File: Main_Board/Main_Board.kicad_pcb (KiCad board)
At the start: 4 copper layers, 66 parts, among them IC1 AZ1085CD-3.3TRG1, J1 PJ-037A, U1 STM32L152ZCTx, U2 LM386, Y1 ABM10W-16.0000MHZ-4-B1U-T3

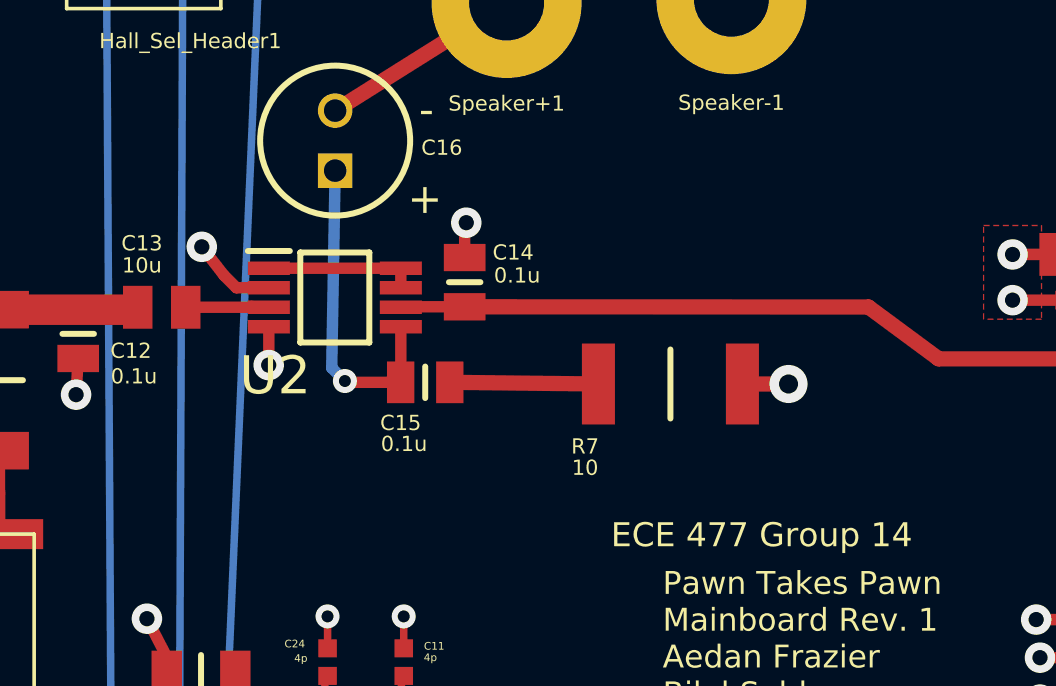
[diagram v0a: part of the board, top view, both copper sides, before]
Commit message: changed LM386 package to match what I bought
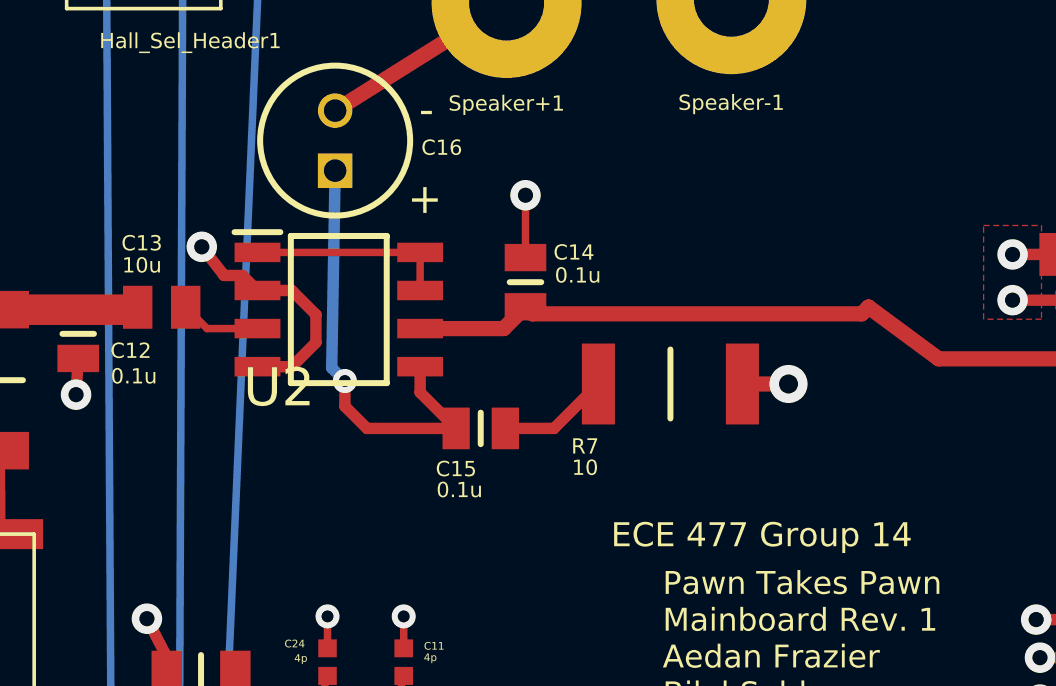
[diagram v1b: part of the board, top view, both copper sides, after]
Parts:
- U2: footprint SamacSys_Parts:SOP65P490X110-8N -> SamacSys_Parts:SOIC127P600X175-8N
- moved C15 2.41 mm to (120.4, 42.1)
- moved C14 2.03 mm to (121.9, 37.2)
- moved U2 0.42 mm to (115.7, 38.1)
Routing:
- net GND: track 154.7 -> 159.4 mm, vias 44 -> 43
- net Net-(C15-Pad1): track 10.9 -> 14.7 mm
- net NC: track 5.05 -> 6.69 mm
- net Net-(C15-Pad2): track 5.08 -> 3.84 mm

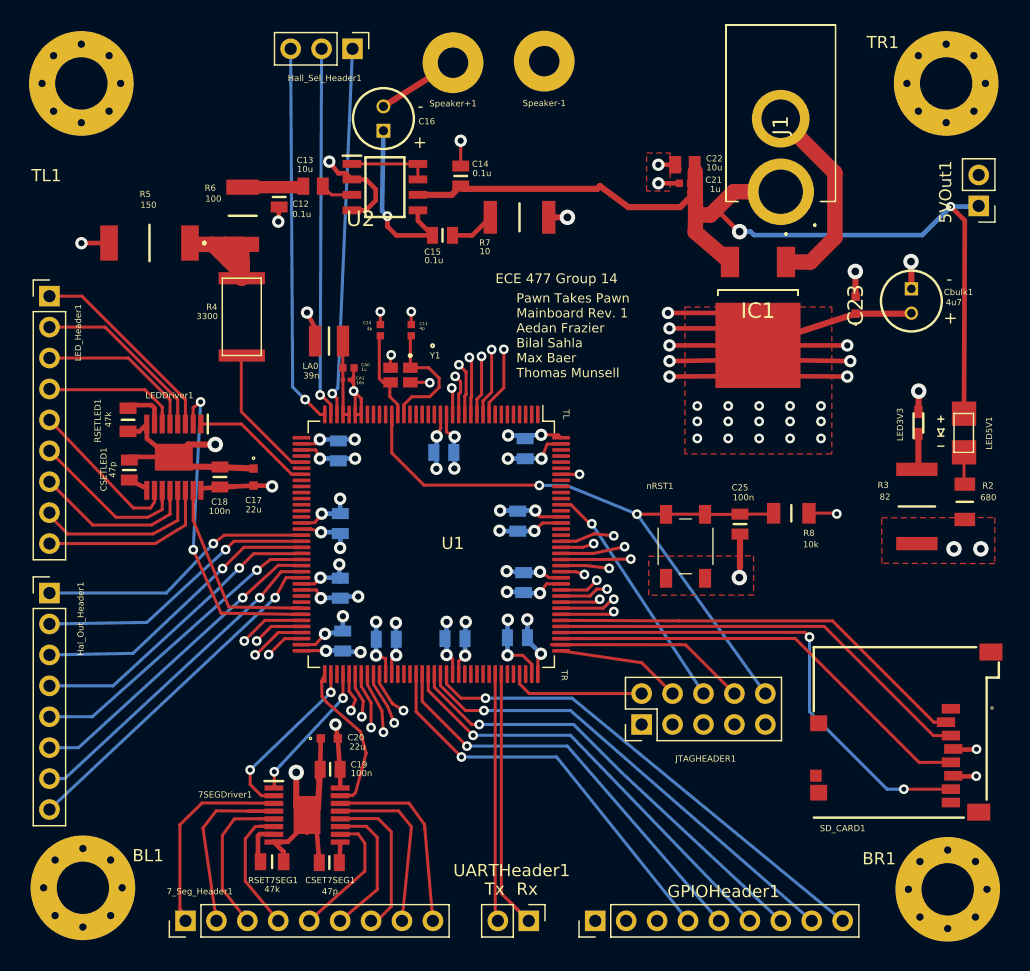
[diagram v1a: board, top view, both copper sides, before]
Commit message: changed board outline
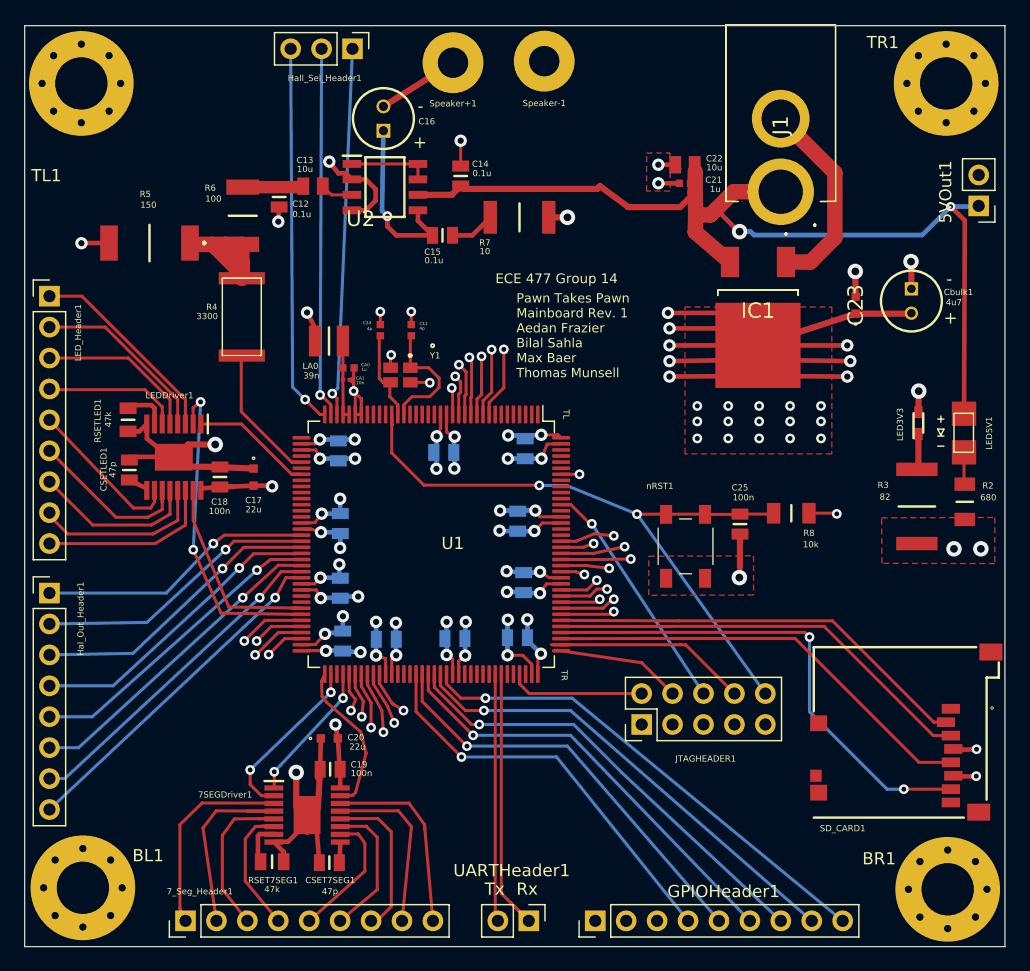
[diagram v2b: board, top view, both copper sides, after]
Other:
- board outline added: 80.5 x 75.6 mm
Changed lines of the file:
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@@
   (general
     (thickness 1.6)
-    (drawings 15)
+    (drawings 19)
     (tracks 847)
     (zones 0)
@@
     (38 B.Mask user)
     (39 F.Mask user)
-    (40 Dwgs.User user)
+    (40 Dwgs.User user hide)
     (41 Cmts.User user)
     (42 Eco1.User user hide)
@@
     )
   )
+  (gr_line (start 86.106 100.4824) (end 86.106 24.8412) (layer Edge.Cuts) (width 0.05))
+  (gr_line (start 166.624 100.4824) (end 86.106 100.4824) (layer Edge.Cuts) (width 0.05))
+  (gr_line (start 166.624 24.8412) (end 166.624 100.4824) (layer Edge.Cuts) (width 0.05))
+  (gr_line (start 86.106 24.8412) (end 166.624 24.8412) (layer Edge.Cuts) (width 0.05))
   (gr_text "ECE 477 Group 14" (at 129.794 45.6184) (layer F.SilkS)
     (effects (font (size 0.8 0.8) (thickness 0.15)))

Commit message: Schem Pictures
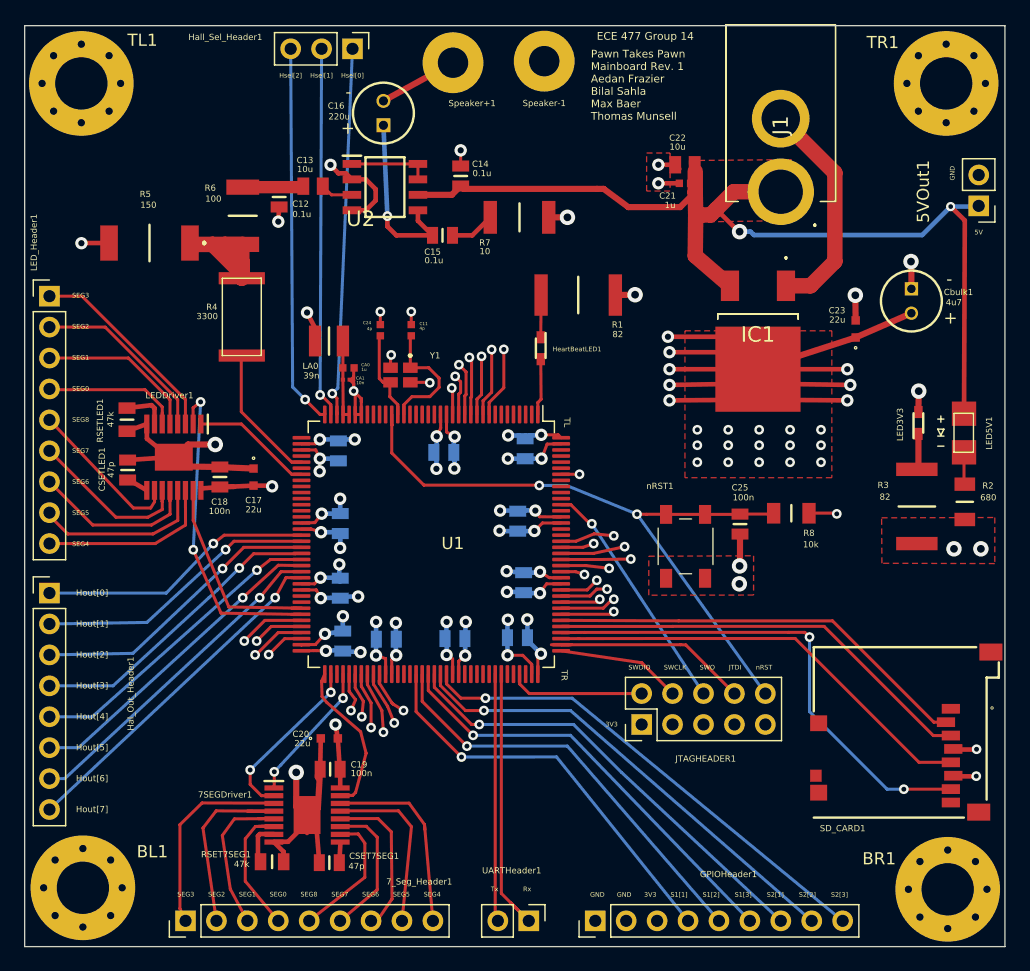
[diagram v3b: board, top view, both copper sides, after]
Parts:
- added HeartBeatLED1: HeartBeatLED, LEDM168X65N, F.Cu at (128.5, 51.3)
- added R1: 82, RESC6432X65N, F.Cu at (131.6, 47.0)
- nRST1: value PTS647SM50SMTR2LFS -> A
- moved C23 1.96 mm to (154.4, 49.8)
- moved IC1 1.96 mm to (146.3, 51.6)
- moved C16 0.45 mm to (115.6, 33.0)
- moved CSETLED1 0.14 mm to (94.6, 61.3)
- moved RSETLED1 0.09 mm to (94.5, 57.2)
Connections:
- U1 pad 1: Net-(U1-Pad1) -> HeartbeatLED
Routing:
- net HeartbeatLED: track 0.00 -> 4.65 mm
- net Net-(HeartBeatLED1-Pad1): track 0.00 -> 3.47 mm
- net GND: track 159.4 -> 162.0 mm, vias 43 -> 45
- net +5V: track 81.8 -> 83.6 mm
- net Net-(C16-Pad2): track 7.05 -> 6.52 mm
- added copper zone on F.Cu, net +5V
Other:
- board text added: "3V3"
- board text added: "5V"
- board text added: "GND"
- board text added: "Hout[0]"
- board text added: "Hout[1]"
- board text added: "Hout[2]"
- board text added: "Hout[3]"
- board text added: "Hout[4]"
- board text added: "Hout[5]"
- board text added: "Hout[6]"
- board text added: "Hout[7]"
- board text added: "Hsel[0]"
- board text added: "Hsel[1]"
- board text added: "Hsel[2]"
- board text added: "JTDI"
- board text added: "S1[1]"
- board text added: "S1[2]"
- board text added: "S1[3]"
- board text added: "S2[1]"
- board text added: "S2[2]"
- board text added: "S2[3]"
- board text added: "SEG0"
- board text added: "SEG1"
- board text added: "SEG2"
- board text added: "SEG3"
- board text added: "SEG4"
- board text added: "SEG5"
- board text added: "SEG6"
- board text added: "SEG7"
- board text added: "SEG8"
- board text added: "SWCLK"
- board text added: "SWDIO"
- board text added: "SWO"
- board text added: "nRST"

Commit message: through hole vias
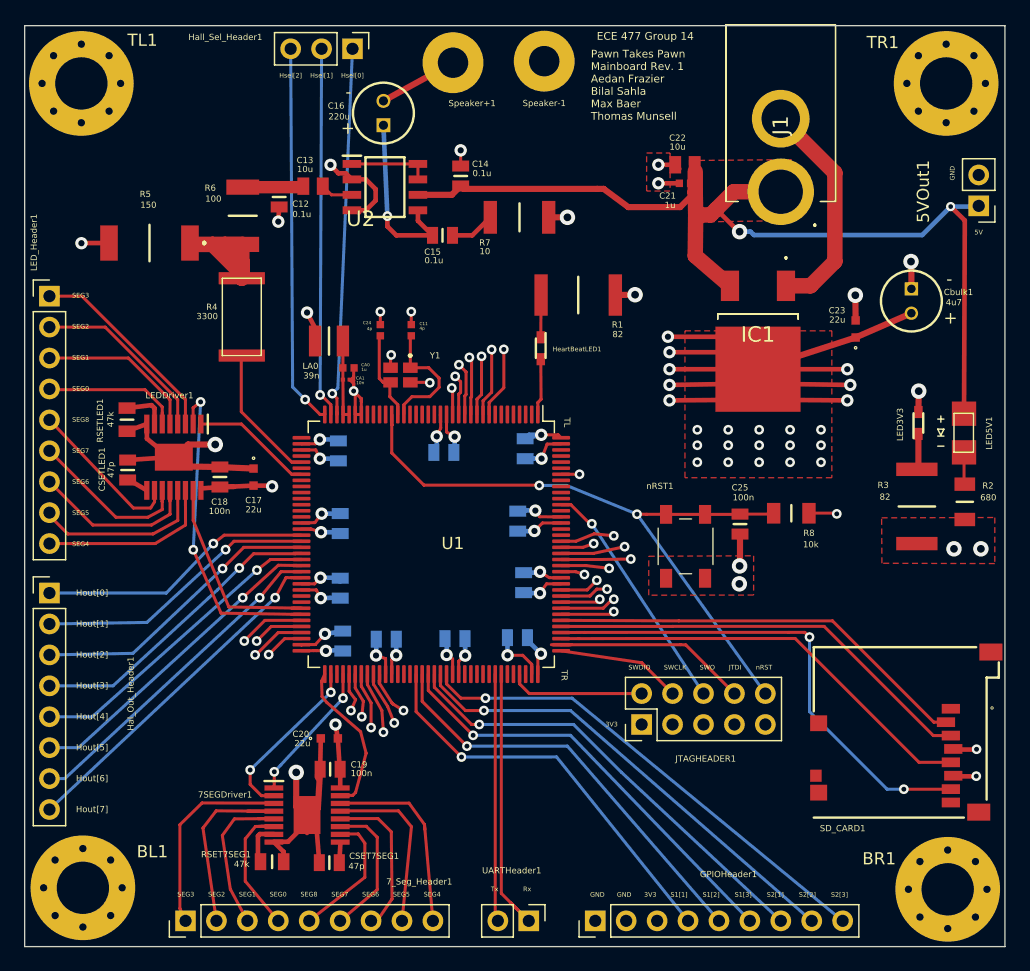
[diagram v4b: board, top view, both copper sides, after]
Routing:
- net GND: track 162.0 -> 147.3 mm, vias 45 -> 34
- net +3V3: track 162.8 -> 148.7 mm, vias 51 -> 40

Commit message: More screenshots
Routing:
- net GND: track 147.3 -> 145.7 mm

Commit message: Reset_Line
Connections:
- GPIOHeader1 pad 1: GND -> Reset_Line
- U1 pad 87: Net-(U1-Pad87) -> Reset_Line
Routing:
- net Reset_Line: track 0.00 -> 30.9 mm, vias 0 -> 1
- net Net-(U1-Pad82): track 3.83 -> 2.66 mm
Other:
- board text added: "Reset_Line"
